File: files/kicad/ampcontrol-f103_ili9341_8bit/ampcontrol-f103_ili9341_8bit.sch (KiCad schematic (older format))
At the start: 61 parts, among them J1 Audio, J10 Buttons, J11 Encoder, J12 TFT, J13 I2C_Audio, J14 I2C_Tuner, J15 I2C_Ext, J2 MUTE_STBY, J3 UART, J4 USB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

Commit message: Arrange components on PCB
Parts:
- removed J10: Buttons, symbol Connector_Generic:Conn_02x06_Counter_Clockwise
- removed J11: Encoder, symbol Connector_Generic:Conn_02x03_Counter_Clockwise
- added J10: Buttons, Connector_PinHeader_2.54mm:PinHeader_2x06_P2.54mm_Vertical, symbol Connector_Generic:Conn_02x06_Odd_Even
- added J11: Encoder, Connector_PinHeader_2.54mm:PinHeader_2x03_P2.54mm_Vertical, symbol Connector_Generic:Conn_02x03_Odd_Even
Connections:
- net BTN_0: now also J10.1 (Pin_1)
- net BTN_1: now also J10.3 (Pin_3)
- net BTN_2: now also J10.5 (Pin_5)
- net BTN_3: now also J10.7 (Pin_7)
- net BTN_4: now also J10.9 (Pin_9)
- net BTN_5: now also J10.11 (Pin_11), J11.5 (Pin_5)
- net ENC_A: now also J11.1 (Pin_1)
- net ENC_B: now also J11.3 (Pin_3)
- net GNDD: now also J10.10 (Pin_10), J10.12 (Pin_12), J10.2 (Pin_2), J10.4 (Pin_4), J10.6 (Pin_6), J10.8 (Pin_8), J11.2 (Pin_2), J11.4 (Pin_4), J11.6 (Pin_6)
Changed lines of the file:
@@
 	0    -1   -1   0
-$EndComp
-$Comp
-L Connector_Generic:Conn_02x03_Odd_Even J8
-U 1 1 5C39890C
-P 5350 1300
-F 0 "J8" H 5400 1500 50  0000 C CNN
-F 1 "BOOT" H 5400 1100 50  0000 C CNN
-F 2 "Connector_PinHeader_2.54mm:PinHeader_2x03_P2.54mm_Vertical" H 5350 1300 50  0001 C CNN
-F 3 "~" H 5350 1300 50  0001 C CNN
-	1    5350 1300
-	1    0    0    -1
 $EndComp
 Wire Wire Line
@@
 Wire Wire Line
 	7350 1550 7350 1600
-$Comp
-L Connector_Generic:Conn_02x06_Counter_Clockwise J10
-U 1 1 5DA69684
-P 8500 4050
-F 0 "J10" H 8550 4350 50  0000 C CNN
-F 1 "Buttons" H 8550 3650 50  0000 C CNN
-F 2 "" H 8500 4050 50  0001 C CNN
-F 3 "~" H 8500 4050 50  0001 C CNN
-	1    8500 4050
-	1    0    0    -1
-$EndComp
 Wire Wire Line
 	8300 3850 8000 3850
@@
 Wire Wire Line
 	8900 3950 8900 4050
-$Comp
-L Connector_Generic:Conn_02x03_Counter_Clockwise J11
-U 1 1 5DC50FD0
-P 8500 5050
-F 0 "J11" H 8550 5250 50  0000 C CNN
-F 1 "Encoder" H 8550 4850 50  0000 C CNN
-F 2 "" H 8500 5050 50  0001 C CNN
-F 3 "~" H 8500 5050 50  0001 C CNN
-	1    8500 5050
-	1    0    0    -1
-$EndComp
 $Comp
 L power:GNDD #PWR040
@@
 	4500 3550 4500 3600
 Connection ~ 4500 3600
+$Comp
+L Connector_Generic:Conn_02x06_Odd_Even J10
+U 1 1 5C3D33A1
+P 8500 4050
+F 0 "J10" H 8550 4350 50  0000 C CNN
+F 1 "Buttons" H 8550 3650 50  0000 C CNN
+F 2 "Connector_PinHeader_2.54mm:PinHeader_2x06_P2.54mm_Vertical" H 8500 4050 50  0001 C CNN
+F 3 "~" H 8500 4050 50  0001 C CNN
+	1    8500 4050
+	1    0    0    -1
+$EndComp
+$Comp
+L Connector_Generic:Conn_02x03_Odd_Even J11
+U 1 1 5C3D396A
+P 8500 5050
+F 0 "J11" H 8550 5250 50  0000 C CNN
+F 1 "Encoder" H 8550 4850 50  0000 C CNN
+F 2 "Connector_PinHeader_2.54mm:PinHeader_2x03_P2.54mm_Vertical" H 8500 5050 50  0001 C CNN
+F 3 "~" H 8500 5050 50  0001 C CNN
+	1    8500 5050
+	1    0    0    -1
+$EndComp
+$Comp
+L Connector_Generic:Conn_02x03_Odd_Even J8
+U 1 1 5C3D402F
+P 5350 1300
+F 0 "J8" H 5400 1500 50  0000 C CNN
+F 1 "BOOT" H 5400 1100 50  0000 C CNN
+F 2 "Connector_PinHeader_2.54mm:PinHeader_2x03_P2.54mm_Vertical" H 5350 1300 50  0001 C CNN
+F 3 "~" H 5350 1300 50  0001 C CNN
+	1    5350 1300
+	1    0    0    -1
+$EndComp
 $EndSCHEMATC

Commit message: Testing autorouted board
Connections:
- net VBAT: now reaches BT1.1 (+), U2.1 (VBAT)
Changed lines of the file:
@@
 	1    0    0    -1
 $EndComp
+Text Label 4750 3600 0    50   ~ 0
+VBAT
 $EndSCHEMATC

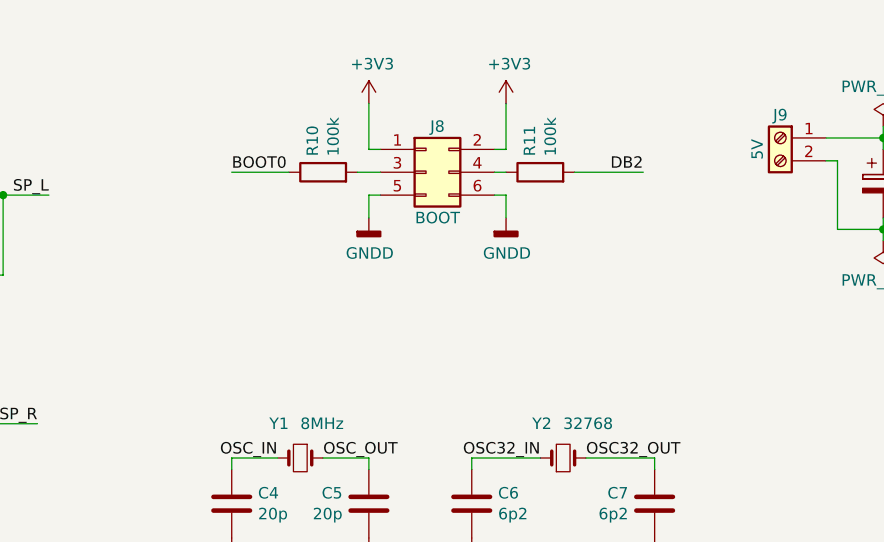
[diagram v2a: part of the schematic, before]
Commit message: Change boot configuration no schematic
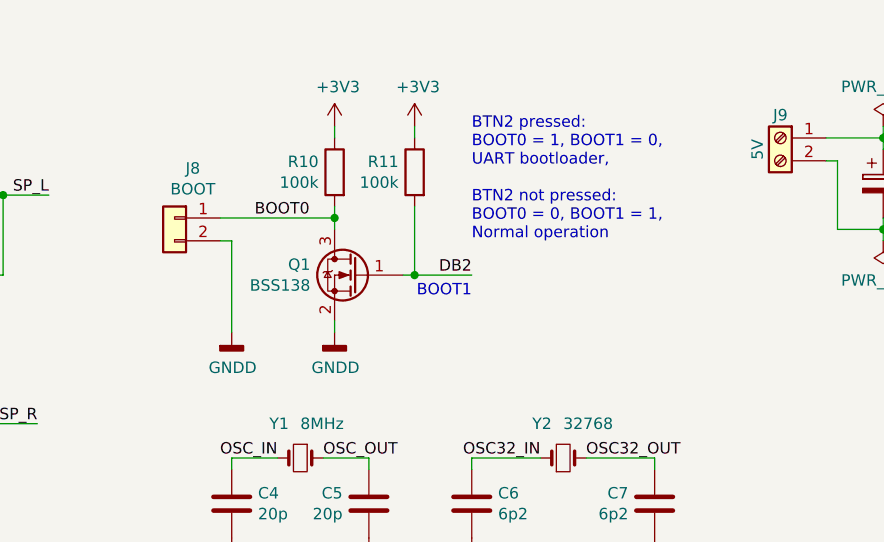
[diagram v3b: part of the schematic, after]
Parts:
- removed J8: BOOT, Connector_PinHeader_2.54mm:PinHeader_2x03_P2.54mm_Vertical, symbol Connector_Generic:Conn_02x03_Odd_Even
- added J8: BOOT, Connector_PinHeader_2.54mm:PinHeader_1x02_P2.54mm_Vertical, symbol Connector_Generic:Conn_01x02
- added Q1: BSS138, Package_TO_SOT_SMD:SOT-23, symbol Transistor_FET:BSS138
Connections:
- net +3V3: now also R10.1, R11.1
- net BOOT0: now also R10.2, J8.1 (Pin_1), Q1.3 (D); no longer R10.1
- net DB2: now also Q1.1 (G)
- net GNDD: now also J8.2 (Pin_2), Q1.2 (S)
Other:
- note added: "BOOT1"
- note added: "BTN2 pressed:\nBOOT0 = 1, BOOT1 = 0,\nUART bootloader,\n\nBTN2 not pressed:\nBOOT0 = 0, BOOT1 = 1,\nNormal operation\n"
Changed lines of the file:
@@
 Text Label 3650 2400 2    50   ~ 0
 SP_R
-Connection ~ 3500 1400
 Connection ~ 3450 2400
 Wire Wire Line
@@
 Text Label 9900 5250 0    50   ~ 0
 DB15
-$Comp
-L Device:R R10
-U 1 1 5C398138
-P 4900 1300
-F 0 "R10" H 4970 1346 50  0000 L CNN
-F 1 "100k" H 4970 1255 50  0000 L CNN
-F 2 "Resistor_SMD:R_1206_3216Metric" V 4830 1300 50  0001 C CNN
-F 3 "~" H 4900 1300 50  0001 C CNN
-	1    4900 1300
-	0    -1   -1   0
-$EndComp
-Wire Wire Line
-	5050 1300 5150 1300
-$Comp
-L Device:R R11
-U 1 1 5C3A1C50
-P 5850 1300
-F 0 "R11" H 5920 1346 50  0000 L CNN
-F 1 "100k" H 5920 1255 50  0000 L CNN
-F 2 "Resistor_SMD:R_1206_3216Metric" V 5780 1300 50  0001 C CNN
-F 3 "~" H 5850 1300 50  0001 C CNN
-	1    5850 1300
-	0    -1   -1   0
-$EndComp
-Wire Wire Line
-	5700 1300 5650 1300
-$Comp
-L power:+3V3 #PWR025
-U 1 1 5C3AA90B
-P 5100 1000
-F 0 "#PWR025" H 5100 850 50  0001 C CNN
-F 1 "+3V3" H 5115 1173 50  0000 C CNN
-F 2 "" H 5100 1000 50  0001 C CNN
-F 3 "" H 5100 1000 50  0001 C CNN
-	1    5100 1000
-	1    0    0    -1
-$EndComp
-$Comp
-L power:+3V3 #PWR029
-U 1 1 5C3AA960
-P 5700 1000
-F 0 "#PWR029" H 5700 850 50  0001 C CNN
-F 1 "+3V3" H 5715 1173 50  0000 C CNN
-F 2 "" H 5700 1000 50  0001 C CNN
-F 3 "" H 5700 1000 50  0001 C CNN
-	1    5700 1000
-	1    0    0    -1
-$EndComp
-Wire Wire Line
-	5100 1000 5100 1200
-Wire Wire Line
-	5100 1200 5150 1200
-Wire Wire Line
-	5700 1000 5700 1200
-$Comp
-L power:GNDD #PWR026
-U 1 1 5C3BC82C
-P 5100 1500
-F 0 "#PWR026" H 5100 1250 50  0001 C CNN
-F 1 "GNDD" H 5104 1345 50  0000 C CNN
-F 2 "" H 5100 1500 50  0001 C CNN
-F 3 "" H 5100 1500 50  0001 C CNN
-	1    5100 1500
-	1    0    0    -1
-$EndComp
-Wire Wire Line
-	5150 1400 5100 1400
-Wire Wire Line
-	5100 1400 5100 1500
-$Comp
-L power:GNDD #PWR030
-U 1 1 5C3EA38D
-P 5700 1500
-F 0 "#PWR030" H 5700 1250 50  0001 C CNN
-F 1 "GNDD" H 5704 1345 50  0000 C CNN
-F 2 "" H 5700 1500 50  0001 C CNN
-F 3 "" H 5700 1500 50  0001 C CNN
-	1    5700 1500
-	1    0    0    -1
-$EndComp
-Wire Wire Line
-	5650 1400 5700 1400
-Wire Wire Line
-	5700 1400 5700 1500
-Wire Wire Line
-	4750 1300 4500 1300
-Text Label 4500 1300 0    50   ~ 0
-BOOT0
-Wire Wire Line
-	6000 1300 6300 1300
-Text Label 6300 1300 2    50   ~ 0
-DB2
-Wire Wire Line
-	5650 1200 5700 1200
 Wire Wire Line
 	5550 2550 5550 2600
@@
 	1    0    0    -1
 $EndComp
-$Comp
-L Connector_Generic:Conn_02x03_Odd_Even J8
-U 1 1 5C3D402F
-P 5350 1300
-F 0 "J8" H 5400 1500 50  0000 C CNN
-F 1 "BOOT" H 5400 1100 50  0000 C CNN
-F 2 "Connector_PinHeader_2.54mm:PinHeader_2x03_P2.54mm_Vertical" H 5350 1300 50  0001 C CNN
-F 3 "~" H 5350 1300 50  0001 C CNN
-	1    5350 1300
-	1    0    0    -1
-$EndComp
 Text Label 4750 3600 0    50   ~ 0
 VBAT
+$Comp
+L Connector_Generic:Conn_01x02 J8
+U 1 1 5C5D17C9
+P 4250 1500
+F 0 "J8" H 4170 1717 50  0000 C CNN
+F 1 "BOOT" H 4170 1626 50  0000 C CNN
+F 2 "Connector_PinHeader_2.54mm:PinHeader_1x02_P2.54mm_Vertical" H 4250 1500 50  0001 C CNN
+F 3 "~" H 4250 1500 50  0001 C CNN
+	1    4250 1500
+	-1   0    0    -1
+$EndComp
+$Comp
+L Transistor_FET:BSS138 Q1
+U 1 1 5C5D1AF1
+P 5050 1750
+F 0 "Q1" H 5256 1796 50  0000 L CNN
+F 1 "BSS138" H 5256 1705 50  0000 L CNN
+F 2 "Package_TO_SOT_SMD:SOT-23" H 5250 1675 50  0001 L CIN
+F 3 "https://www.fairchildsemi.com/datasheets/BS/BSS138.pdf" H 5050 1750 50  0001 L CNN
+	1    5050 1750
+	-1   0    0    -1
+$EndComp
+Wire Wire Line
+	5250 1750 5300 1750
+Text Label 5550 1750 2    50   ~ 0
+DB2
+$Comp
+L Device:R R11
+U 1 1 5C5EED39
+P 5300 1300
+F 0 "R11" H 5370 1346 50  0000 L CNN
+F 1 "100k" H 5370 1255 50  0000 L CNN
+F 2 "Resistor_SMD:R_1206_3216Metric" V 5230 1300 50  0001 C CNN
+F 3 "~" H 5300 1300 50  0001 C CNN
+	1    5300 1300
+	-1   0    0    -1
+$EndComp
+Connection ~ 5300 1750
+Wire Wire Line
+	5300 1750 5550 1750
+$Comp
+L Device:R R10
+U 1 1 5C628F07
+P 4950 1300
+F 0 "R10" H 5020 1346 50  0000 L CNN
+F 1 "100k" H 5020 1255 50  0000 L CNN
+F 2 "Resistor_SMD:R_1206_3216Metric" V 4880 1300 50  0001 C CNN
+F 3 "~" H 4950 1300 50  0001 C CNN
+	1    4950 1300
+	-1   0    0    -1
+$EndComp
+Connection ~ 3500 1400
+Wire Wire Line
+	4950 1450 4950 1500
+Wire Wire Line
+	4450 1500 4950 1500
+Connection ~ 4950 1500
+Wire Wire Line
+	4950 1500 4950 1550
+Wire Wire Line
+	5300 1450 5300 1750
+$Comp
+L power:+3V3 #PWR0101
+U 1 1 5C732A66
+P 4950 1100
+F 0 "#PWR0101" H 4950 950 50  0001 C CNN
+F 1 "+3V3" H 4965 1273 50  0000 C CNN
+F 2 "" H 4950 1100 50  0001 C CNN
+F 3 "" H 4950 1100 50  0001 C CNN
+	1    4950 1100
+	1    0    0    -1
+$EndComp
+Wire Wire Line
+	4950 1100 4950 1150
+$Comp
+L power:+3V3 #PWR0102
+U 1 1 5C750903
+P 5300 1100
+F 0 "#PWR0102" H 5300 950 50  0001 C CNN
+F 1 "+3V3" H 5315 1273 50  0000 C CNN
+F 2 "" H 5300 1100 50  0001 C CNN
+F 3 "" H 5300 1100 50  0001 C CNN
+	1    5300 1100
+	1    0    0    -1
+$EndComp
+Wire Wire Line
+	5300 1100 5300 1150
+Wire Wire Line
+	4450 1600 4500 1600
+Wire Wire Line
+	4500 1600 4500 2000
+Wire Wire Line
+	4950 1950 4950 2000
+$Comp
+L power:GNDD #PWR0103
+U 1 1 5C7C9868
+P 4500 2000
+F 0 "#PWR0103" H 4500 1750 50  0001 C CNN
+F 1 "GNDD" H 4504 1845 50  0000 C CNN
+F 2 "" H 4500 2000 50  0001 C CNN
+F 3 "" H 4500 2000 50  0001 C CNN
+	1    4500 2000
+	1    0    0    -1
+$EndComp
+$Comp
+L power:GNDD #PWR0104
+U 1 1 5C7C98F7
+P 4950 2000
+F 0 "#PWR0104" H 4950 1750 50  0001 C CNN
+F 1 "GNDD" H 4954 1845 50  0000 C CNN
+F 2 "" H 4950 2000 50  0001 C CNN
+F 3 "" H 4950 2000 50  0001 C CNN
+	1    4950 2000
+	1    0    0    -1
+$EndComp
+Text Label 4600 1500 0    50   ~ 0
+BOOT0
+Text Notes 5550 1850 2    50   ~ 0
+BOOT1
+Text Notes 5550 1600 0    50   ~ 0
+BTN2 pressed:\nBOOT0 = 1, BOOT1 = 0,\nUART bootloader,\n\nBTN2 not pressed:\nBOOT0 = 0, BOOT1 = 1,\nNormal operation\n
 $EndSCHEMATC
